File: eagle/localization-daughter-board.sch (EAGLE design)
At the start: 23 parts, among them U1 LM340MP-5.0/NOPB, U2 RPI-ZERO, U3 LMS8117AMP-ADJ/NOPB, U4 TXS0101DCKR, U5 SN65HVD256DR, U6 STM32F042FXP

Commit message: Finished initial design
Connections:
- removed net 3V3: U6.VDD, U6.VDDA
- net +3V3: now also U6.VDD, U6.VDDA
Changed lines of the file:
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@@
 <wire x1="162.56" y1="127" x2="162.56" y2="124.46" width="0.1524" layer="91"/>
 </segment>
-</net>
-<net name="3V3" class="0">
+<segment>
+<pinref part="U6" gate="A" pin="VDDA"/>
+<wire x1="172.72" y1="66.04" x2="162.56" y2="66.04" width="0.1524" layer="91"/>
+<label x="162.56" y="66.04" size="1.778" layer="95"/>
+</segment>
 <segment>
 <pinref part="U6" gate="A" pin="VDD"/>
 <wire x1="215.9" y1="66.04" x2="226.06" y2="66.04" width="0.1524" layer="91"/>
 <label x="226.06" y="66.04" size="1.778" layer="95" rot="MR0"/>
-</segment>
-<segment>
-<pinref part="U6" gate="A" pin="VDDA"/>
-<wire x1="172.72" y1="66.04" x2="162.56" y2="66.04" width="0.1524" layer="91"/>
-<label x="162.56" y="66.04" size="1.778" layer="95"/>
 </segment>
 </net>
@@
 </sheet>
 </sheets>
+<errors>
+</errors>
 </schematic>
 </drawing>

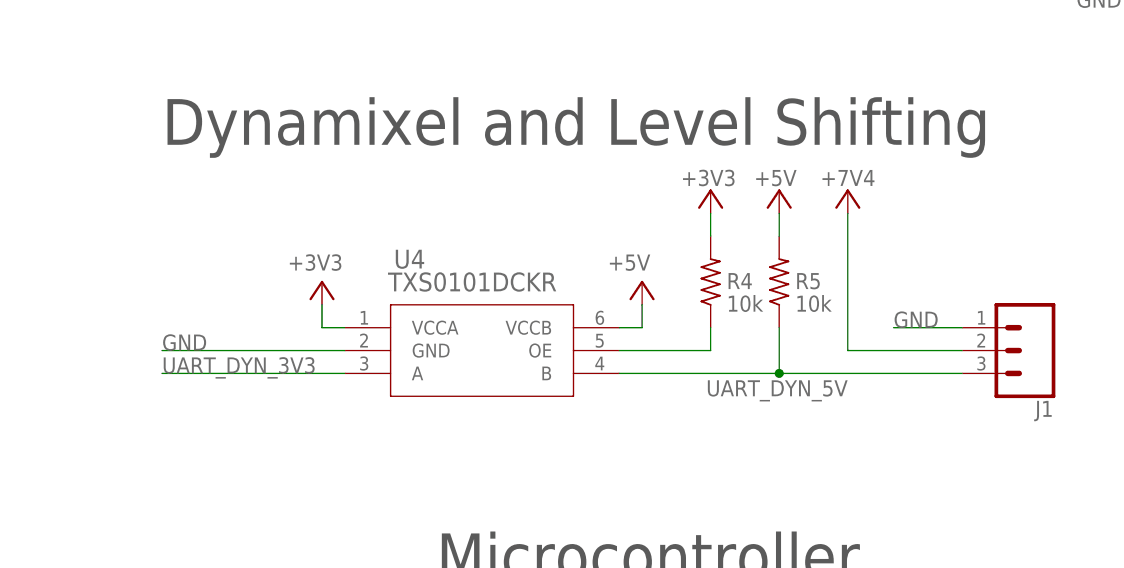
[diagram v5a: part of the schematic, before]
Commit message: Removed redundant pull-up resistor
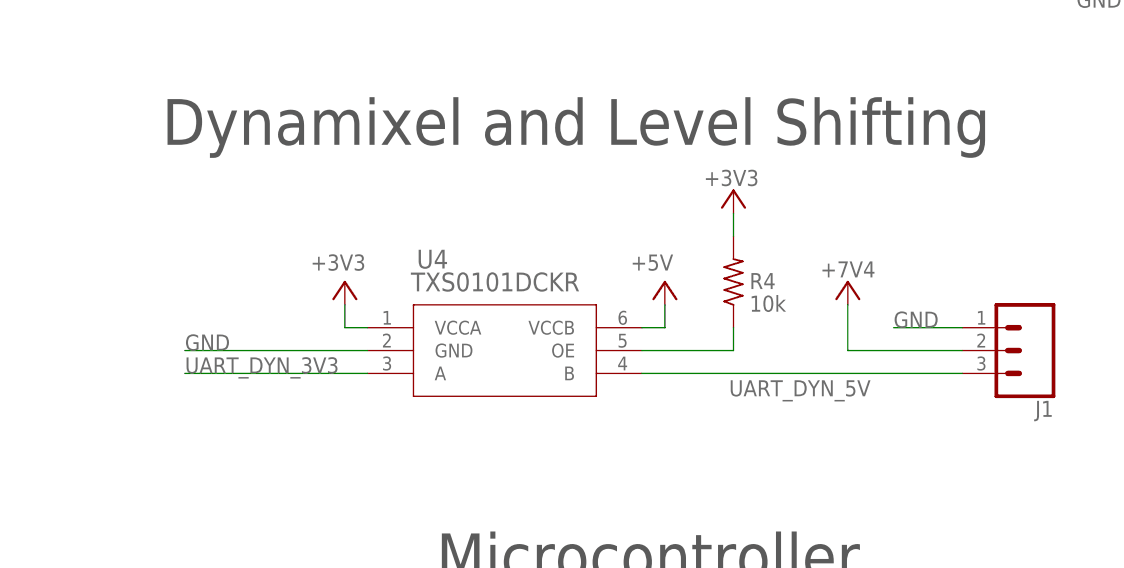
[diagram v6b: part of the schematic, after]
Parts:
- removed R5: 10k, resistor:R-US_R0805
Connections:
- net +5V: no longer R5.2
- net UART_DYN_5V: no longer R5.1
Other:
- moved on the sheet: R4, U4
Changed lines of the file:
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@@
 <part name="GND7" library="supply1" library_urn="urn:adsk.eagle:library:371" deviceset="GND" device=""/>
 <part name="P+10" library="supply1" library_urn="urn:adsk.eagle:library:371" deviceset="VCC" device=""/>
-<part name="R5" library="resistor" library_urn="urn:adsk.eagle:library:348" deviceset="R-US_" device="R0805" package3d_urn="urn:adsk.eagle:package:26059/1" value="10k"/>
-<part name="P+9" library="supply1" library_urn="urn:adsk.eagle:library:371" deviceset="+5V" device=""/>
 <part name="R4" library="resistor" library_urn="urn:adsk.eagle:library:348" deviceset="R-US_" device="R0805" package3d_urn="urn:adsk.eagle:package:26059/1" value="10k"/>
 <part name="+3V33" library="supply1" library_urn="urn:adsk.eagle:library:371" deviceset="+3V3" device=""/>
@@
 <instance part="GND9" gate="1" x="137.16" y="162.56"/>
 <instance part="J1" gate="G$1" x="198.12" y="111.76" rot="R180"/>
-<instance part="U4" gate="A" x="119.38" y="114.3"/>
-<instance part="P+8" gate="1" x="154.94" y="119.38" smashed="yes">
-<attribute name="VALUE" x="151.13" y="120.65" size="1.778" layer="96"/>
-</instance>
-<instance part="+3V32" gate="G$1" x="119.38" y="119.38" smashed="yes">
-<attribute name="VALUE" x="115.57" y="120.65" size="1.778" layer="96"/>
+<instance part="U4" gate="A" x="121.92" y="114.3"/>
+<instance part="P+8" gate="1" x="157.48" y="119.38" smashed="yes">
+<attribute name="VALUE" x="153.67" y="120.65" size="1.778" layer="96"/>
+</instance>
+<instance part="+3V32" gate="G$1" x="121.92" y="119.38" smashed="yes">
+<attribute name="VALUE" x="118.11" y="120.65" size="1.778" layer="96"/>
 </instance>
 <instance part="P+11" gate="1" x="215.9" y="198.12" smashed="yes">
@@
 <instance part="C4" gate="G$1" x="76.2" y="114.3"/>
 <instance part="GND7" gate="1" x="76.2" y="104.14"/>
-<instance part="P+10" gate="VCC" x="177.8" y="129.54" smashed="yes"/>
-<instance part="R5" gate="G$1" x="170.18" y="119.38" smashed="yes" rot="R90">
-<attribute name="NAME" x="171.958" y="118.5926" size="1.778" layer="95"/>
-<attribute name="VALUE" x="171.958" y="116.078" size="1.778" layer="96"/>
-</instance>
-<instance part="P+9" gate="1" x="170.18" y="129.54" smashed="yes">
-<attribute name="VALUE" x="167.386" y="130.048" size="1.778" layer="96"/>
-</instance>
-<instance part="R4" gate="G$1" x="162.56" y="119.38" smashed="yes" rot="R90">
-<attribute name="NAME" x="164.338" y="118.5926" size="1.778" layer="95"/>
-<attribute name="VALUE" x="164.338" y="116.078" size="1.778" layer="96"/>
-</instance>
-<instance part="+3V33" gate="G$1" x="162.56" y="129.54" smashed="yes">
-<attribute name="VALUE" x="159.258" y="130.048" size="1.778" layer="96"/>
+<instance part="P+10" gate="VCC" x="177.8" y="119.38" smashed="yes"/>
+<instance part="R4" gate="G$1" x="165.1" y="119.38" smashed="yes" rot="R90">
+<attribute name="NAME" x="166.878" y="118.5926" size="1.778" layer="95"/>
+<attribute name="VALUE" x="166.878" y="116.078" size="1.778" layer="96"/>
+</instance>
+<instance part="+3V33" gate="G$1" x="165.1" y="129.54" smashed="yes">
+<attribute name="VALUE" x="161.798" y="130.048" size="1.778" layer="96"/>
 </instance>
 <instance part="CR1" gate="A" x="215.9" y="180.34" smashed="yes" rot="R90">
@@
 <segment>
 <pinref part="U4" gate="A" pin="GND"/>
-<wire x1="121.92" y1="111.76" x2="101.6" y2="111.76" width="0.1524" layer="91"/>
-<label x="101.6" y="111.76" size="1.778" layer="95"/>
+<wire x1="124.46" y1="111.76" x2="104.14" y2="111.76" width="0.1524" layer="91"/>
+<label x="104.14" y="111.76" size="1.778" layer="95"/>
 </segment>
 <segment>
@@
 <segment>
 <pinref part="U4" gate="A" pin="VCCB"/>
-<wire x1="152.4" y1="114.3" x2="154.94" y2="114.3" width="0.1524" layer="91"/>
+<wire x1="154.94" y1="114.3" x2="157.48" y2="114.3" width="0.1524" layer="91"/>
 <pinref part="P+8" gate="1" pin="+5V"/>
-<wire x1="154.94" y1="116.84" x2="154.94" y2="114.3" width="0.1524" layer="91"/>
+<wire x1="157.48" y1="116.84" x2="157.48" y2="114.3" width="0.1524" layer="91"/>
 </segment>
 <segment>
@@
 <wire x1="205.74" y1="167.64" x2="220.98" y2="167.64" width="0.1524" layer="91"/>
 </segment>
-<segment>
-<pinref part="P+9" gate="1" pin="+5V"/>
-<pinref part="R5" gate="G$1" pin="2"/>
-<wire x1="170.18" y1="127" x2="170.18" y2="124.46" width="0.1524" layer="91"/>
-</segment>
 </net>
 <net name="+3V3" class="0">
@@
 <segment>
 <pinref part="U4" gate="A" pin="VCCA"/>
-<wire x1="121.92" y1="114.3" x2="119.38" y2="114.3" width="0.1524" layer="91"/>
+<wire x1="124.46" y1="114.3" x2="121.92" y2="114.3" width="0.1524" layer="91"/>
 <pinref part="+3V32" gate="G$1" pin="+3V3"/>
-<wire x1="119.38" y1="116.84" x2="119.38" y2="114.3" width="0.1524" layer="91"/>
+<wire x1="121.92" y1="116.84" x2="121.92" y2="114.3" width="0.1524" layer="91"/>
 </segment>
 <segment>
@@
 <pinref part="+3V33" gate="G$1" pin="+3V3"/>
 <pinref part="R4" gate="G$1" pin="2"/>
-<wire x1="162.56" y1="127" x2="162.56" y2="124.46" width="0.1524" layer="91"/>
+<wire x1="165.1" y1="127" x2="165.1" y2="124.46" width="0.1524" layer="91"/>
 </segment>
 <segment>
@@
 <segment>
 <pinref part="J1" gate="G$1" pin="3"/>
-<wire x1="190.5" y1="109.22" x2="170.18" y2="109.22" width="0.1524" layer="91"/>
-<label x="177.8" y="106.68" size="1.778" layer="95" rot="MR0"/>
+<wire x1="190.5" y1="109.22" x2="154.94" y2="109.22" width="0.1524" layer="91"/>
+<label x="180.34" y="106.68" size="1.778" layer="95" rot="MR0"/>
 <pinref part="U4" gate="A" pin="B"/>
-<wire x1="152.4" y1="109.22" x2="170.18" y2="109.22" width="0.1524" layer="91"/>
-<pinref part="R5" gate="G$1" pin="1"/>
-<wire x1="170.18" y1="114.3" x2="170.18" y2="109.22" width="0.1524" layer="91"/>
-<junction x="170.18" y="109.22"/>
 </segment>
 </net>
@@
 <segment>
 <pinref part="U4" gate="A" pin="OE"/>
-<wire x1="152.4" y1="111.76" x2="162.56" y2="111.76" width="0.1524" layer="91"/>
+<wire x1="154.94" y1="111.76" x2="165.1" y2="111.76" width="0.1524" layer="91"/>
 <pinref part="R4" gate="G$1" pin="1"/>
-<wire x1="162.56" y1="114.3" x2="162.56" y2="111.76" width="0.1524" layer="91"/>
+<wire x1="165.1" y1="114.3" x2="165.1" y2="111.76" width="0.1524" layer="91"/>
 </segment>
 </net>
@@
 <segment>
 <pinref part="U4" gate="A" pin="A"/>
-<wire x1="121.92" y1="109.22" x2="101.6" y2="109.22" width="0.1524" layer="91"/>
-<label x="101.6" y="109.22" size="1.778" layer="95"/>
+<wire x1="124.46" y1="109.22" x2="104.14" y2="109.22" width="0.1524" layer="91"/>
+<label x="104.14" y="109.22" size="1.778" layer="95"/>
 </segment>
 <segment>
@@
 <segment>
 <pinref part="P+10" gate="VCC" pin="VCC"/>
-<wire x1="177.8" y1="127" x2="177.8" y2="111.76" width="0.1524" layer="91"/>
+<wire x1="177.8" y1="116.84" x2="177.8" y2="111.76" width="0.1524" layer="91"/>
 <pinref part="J1" gate="G$1" pin="2"/>
 <wire x1="177.8" y1="111.76" x2="190.5" y2="111.76" width="0.1524" layer="91"/>
-<label x="174.752" y="130.048" size="1.778" layer="95"/>
-</segment>
-</net>
+<label x="174.752" y="119.888" size="1.778" layer="95"/>
+</segment>
+</net>
